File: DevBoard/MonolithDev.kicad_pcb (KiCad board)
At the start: 2 copper layers, 0 parts

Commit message: Dev board: board setup (175x115, 4L 0.8 mm), netlist loaded, PDFN fix
- Board: 175 x 115 mm (the four holders need ~96 x 110), 4 layers 0.8 mm,
  2 oz outer / 1 oz inner, ENIG stack-up; six M3 board-only holes; outline
  broken for the two USB-C notches, J401/J501 placed and locked on the right edge
- JLC rules, via/track presets, net classes (HighCurrent, Power, GND,
  GateDrive) and custom rules in MonolithDev.kicad_dru (tools/setup_board.py)
- Netlist loaded with tools/netlist_to_board.py (the MCP sync merged the two
  ports' nets); kicad-cli parity check reports 0 issues
- Q101/Q102: AGM404AP1 is a 3.3x3.3 PDFN, not TDSON-8 (5x6); new footprint
- USB-C signal pads moved 0.2 mm in from the notch for JLC's edge clearance
- Production notes: notch is 5.65 mm deep (not 4.7), flange sticks out ~1.95 mm

Co-Authored-By: Claude Opus 5.5 <noreply@anthropic.com>
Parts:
- added BT101, BT102, BT103, BT104: BH-21700-B1BJ001, MonolithDev:BatteryHolder_MYOUNG_BH-21700-B1BJ001, F.Cu at (0.00, 0.00)
- added C101, C102, C103, C104, C412, C413, C440, C512, C513, C540: 0.1u 25V, Capacitor_SMD:C_0603_1608Metric, F.Cu at (0.00, 0.00)
- added C105: 2.2u 25V, Capacitor_SMD:C_0603_1608Metric, F.Cu at (0.00, 0.00)
- added C106, C202, C203, C308, C309, C310, C311: 0.1u, Capacitor_SMD:C_0603_1608Metric, F.Cu at (0.00, 0.00)
- added C107, C108, C415, C416, C418, C419, C430, C438, C446, C515, C516, C518, C519, C530, C538, C546: 0.1u 50V, Capacitor_SMD:C_0603_1608Metric, F.Cu at (0.00, 0.00)
- added C201: 22n DNP, Capacitor_SMD:C_0603_1608Metric, F.Cu at (0.00, 0.00)
- added C204: 1u 50V, Capacitor_SMD:C_0805_2012Metric, F.Cu at (0.00, 0.00)
- added C205: 2.2u 10V, Capacitor_SMD:C_0603_1608Metric, F.Cu at (0.00, 0.00)
- added C206: 2.2u 50V, Capacitor_SMD:C_0805_2012Metric, F.Cu at (0.00, 0.00)
- added C207: 22u 10V, Capacitor_SMD:C_0805_2012Metric, F.Cu at (0.00, 0.00)
- added C301: 4.7u, Capacitor_SMD:C_0603_1608Metric, F.Cu at (0.00, 0.00)
- added C302, C303, C304, C408, C508: 0.1u, Capacitor_SMD:C_0402_1005Metric, F.Cu at (0.00, 0.00)
- added C401, C402, C501, C502: 330p, Capacitor_SMD:C_0402_1005Metric, F.Cu at (0.00, 0.00)
- added C403, C404, C503, C504: 10u 25V, Capacitor_SMD:C_0805_2012Metric, F.Cu at (0.00, 0.00)
- added C405, C505: 10u 10V, Capacitor_SMD:C_0603_1608Metric, F.Cu at (0.00, 0.00)
- added C406, C506: 4.7u 50V, Capacitor_SMD:C_0805_2012Metric, F.Cu at (0.00, 0.00)
- added C407, C507: 10u 10V, Capacitor_SMD:C_0805_2012Metric, F.Cu at (0.00, 0.00)
- added C409, C509: 1u 35V (VAC), Capacitor_SMD:C_0603_1608Metric, F.Cu at (0.00, 0.00)
- added C410, C411, C510, C511: 4.7u 16V, Capacitor_SMD:C_0805_2012Metric, F.Cu at (0.00, 0.00)
- added C414, C417, C514, C517: 0.47u 25V, Capacitor_SMD:C_0603_1608Metric, F.Cu at (0.00, 0.00)
- added C420, C421, C422, C423, C424, C425, C426, C427, C428, C429, C520, C521, C522, C523, C524, C525, C526, C527, C528, C529: 22u 35V, Capacitor_SMD:C_1210_3225Metric, F.Cu at (0.00, 0.00)
- added C431, C432, C433, C434, C435, C436, C437, C531, C532, C533, C534, C535, C536, C537: 47u 25V, Capacitor_SMD:C_1210_3225Metric, F.Cu at (0.00, 0.00)
- added C439, C539: 33n, Capacitor_SMD:C_0603_1608Metric, F.Cu at (0.00, 0.00)
- added C441, C442, C541, C542: 22u 35V, Capacitor_SMD:C_1206_3216Metric, F.Cu at (0.00, 0.00)
- added C443, C543: 220u 16V, Capacitor_SMD:CP_Elec_6.3x7.7, F.Cu at (0.00, 0.00)
- added C444, C445, C544, C545: 10u 50V, Capacitor_SMD:C_1206_3216Metric, F.Cu at (0.00, 0.00)
- added D101: BAT54WS, Diode_SMD:D_SOD-323, F.Cu at (0.00, 0.00)
- added D301: Green status, LED_SMD:LED_0603_1608Metric, F.Cu at (0.00, 0.00)
- added D401, D501: SMAJ22A, Diode_SMD:D_SMA, F.Cu at (0.00, 0.00)
- added D402, D403, D502, D503: ESD2CAN24DBZRQ1, Package_TO_SOT_SMD:SOT-23, F.Cu at (0.00, 0.00)
- added F101: 8A 32V, Fuse:Fuse_1206_3216Metric, F.Cu at (0.00, 0.00)
- added H1: MountingHole_3.2mm_M3, MountingHole:MountingHole_3.2mm_M3, F.Cu at (54.0, 54.0)
- added H2: MountingHole_3.2mm_M3, MountingHole:MountingHole_3.2mm_M3, F.Cu at (151.0, 54.0)
- added H3: MountingHole_3.2mm_M3, MountingHole:MountingHole_3.2mm_M3, F.Cu at (221.0, 54.0)
- added H4: MountingHole_3.2mm_M3, MountingHole:MountingHole_3.2mm_M3, F.Cu at (54.0, 161.0)
- added H5: MountingHole_3.2mm_M3, MountingHole:MountingHole_3.2mm_M3, F.Cu at (151.0, 161.0)
- added H6: MountingHole_3.2mm_M3, MountingHole:MountingHole_3.2mm_M3, F.Cu at (221.0, 161.0)
- added J101: Pack (welded 4S) - use instead of holders, TerminalBlock_Phoenix:TerminalBlock_Phoenix_MKDS-1,5-5-5.08_1x05_P5.08mm_Horizontal, F.Cu at (0.00, 0.00)
- added J102: Cell NTC 10k 103AT, Connector_PinHeader_2.54mm:PinHeader_1x02_P2.54mm_Vertical, F.Cu at (0.00, 0.00)
- added J103: EV2400 SMBus, Connector_PinHeader_2.54mm:PinHeader_1x03_P2.54mm_Vertical, F.Cu at (0.00, 0.00)
- added J201: SMA OUT_LO, Connector_Coaxial:SMA_Amphenol_132289_EdgeMount, F.Cu at (0.00, 0.00)
- added J202: SMA OUT_HI, Connector_Coaxial:SMA_Amphenol_132289_EdgeMount, F.Cu at (0.00, 0.00)
- added J301: SWD, Connector_PinHeader_1.27mm:PinHeader_2x05_P1.27mm_Vertical, F.Cu at (0.00, 0.00)
- added J302: UART debug, Connector_PinHeader_2.54mm:PinHeader_1x03_P2.54mm_Vertical, F.Cu at (0.00, 0.00)
- added J303: Spare GPIO, Connector_PinHeader_2.54mm:PinHeader_1x07_P2.54mm_Vertical, F.Cu at (0.00, 0.00)
- added J401: TYPE-C 16PCB0.8 IP68, MonolithDev:USB_C_Receptacle_ShouHan_TYPE-C_16PCB0.8_IP68, F.Cu at (225.0, 85.0)
- added J402, J502: I2CC logic analyzer, Connector_PinHeader_2.54mm:PinHeader_1x03_P2.54mm_Vertical, F.Cu at (0.00, 0.00)
- added J501: TYPE-C 16PCB0.8 IP68, MonolithDev:USB_C_Receptacle_ShouHan_TYPE-C_16PCB0.8_IP68, F.Cu at (225.0, 128.0)
- added JP201: AMP_EN, Connector_PinHeader_2.54mm:PinHeader_1x02_P2.54mm_Vertical, F.Cu at (0.00, 0.00)
- added JP202: Meas. section power, Connector_PinHeader_2.54mm:PinHeader_1x02_P2.54mm_Vertical, F.Cu at (0.00, 0.00)
- added L201: 10u, Inductor_SMD:L_Bourns-SRN4018, F.Cu at (0.00, 0.00)
- added L401, L501: 2.2u, Inductor_SMD:L_Coilcraft_XAL7030-222, F.Cu at (0.00, 0.00)
- added L402, L502: 3.3u, Inductor_SMD:L_Bourns_SRP5030T, F.Cu at (0.00, 0.00)
- added Q101, Q102: AGM404AP1, MonolithDev:AGM_PDFN-8_3.3x3.3mm_P0.65mm, F.Cu at (0.00, 0.00)
- added Q401, Q402, Q501, Q502: IAUC45N04S6L063H, MonolithDev:Infineon_PG-TDSON-8-57_HalfBridge, F.Cu at (0.00, 0.00)
- added R1, R2, R202, R203, R204, R205, R3, R307, R4: 0R, Resistor_SMD:R_0603_1608Metric, F.Cu at (0.00, 0.00)
- added R101, R102, R103, R104, R105, R106, R107, R108, R115, R116: 100, Resistor_SMD:R_0603_1608Metric, F.Cu at (0.00, 0.00)
- added R109, R111: 5.1k, Resistor_SMD:R_0603_1608Metric, F.Cu at (0.00, 0.00)
- added R110, R112: 10M, Resistor_SMD:R_0603_1608Metric, F.Cu at (0.00, 0.00)
- added R113, R302, R404, R417, R421, R422, R423, R504, R517, R521, R522, R523: 10k, Resistor_SMD:R_0603_1608Metric, F.Cu at (0.00, 0.00)
- added R114, R206, R208, R432, R532: 100k, Resistor_SMD:R_0603_1608Metric, F.Cu at (0.00, 0.00)
- added R201: 10R 1% 0.5W, Resistor_SMD:R_1206_3216Metric, F.Cu at (0.00, 0.00)
- added R207, R301, R401, R501: 0R, Resistor_SMD:R_0805_2012Metric, F.Cu at (0.00, 0.00)
- added R303: 0R, Resistor_SMD:R_0402_1005Metric, F.Cu at (0.00, 0.00)
- added R304, R305: 4.7k, Resistor_SMD:R_0603_1608Metric, F.Cu at (0.00, 0.00)
- added R306: 1k, Resistor_SMD:R_0603_1608Metric, F.Cu at (0.00, 0.00)
- added R308, R309, R310, R311, R411, R419, R511, R519: 10.0k 0.1%, Resistor_SMD:R_0805_2012Metric, F.Cu at (0.00, 0.00)
- added R402, R403, R502, R503: 3.3k, Resistor_SMD:R_0603_1608Metric, F.Cu at (0.00, 0.00)
- added R405, R406, R407, R408, R505, R506, R507, R508: DNP, Resistor_SMD:R_0603_1608Metric, F.Cu at (0.00, 0.00)
- added R409, R509: 137k 0.1%, Resistor_SMD:R_0805_2012Metric, F.Cu at (0.00, 0.00)
- added R410, R412, R510, R512: 40.2k 0.1%, Resistor_SMD:R_0805_2012Metric, F.Cu at (0.00, 0.00)
- added R413, R416, R513, R516: 5.11k 0.1%, Resistor_SMD:R_0603_1608Metric, F.Cu at (0.00, 0.00)
- added R414, R514: 3.65k 0.1%, Resistor_SMD:R_0603_1608Metric, F.Cu at (0.00, 0.00)
- added R415, R515: 1.74k 0.1%, Resistor_SMD:R_0603_1608Metric, F.Cu at (0.00, 0.00)
- added R418, R518: 100k 0.1%, Resistor_SMD:R_0805_2012Metric, F.Cu at (0.00, 0.00)
- added R420, R425, R426, R428, R429, R520, R525, R526, R528, R529: 10R, Resistor_SMD:R_0603_1608Metric, F.Cu at (0.00, 0.00)
- added R424, R524: 5m 2W (RAC), Resistor_SMD:R_2010_5025Metric, F.Cu at (0.00, 0.00)
- added R427, R527: 5m 2W (RBAT), Resistor_SMD:R_2010_5025Metric, F.Cu at (0.00, 0.00)
- added R430, R530: Link 10A, MonolithDev:NetTie-2_SMD_3x3mm_Bridge3mm, F.Cu at (0.00, 0.00)
- added R431, R531: 0R, Resistor_SMD:R_1206_3216Metric, F.Cu at (0.00, 0.00)
- added R433, R533: 105k 0.1%, Resistor_SMD:R_0805_2012Metric, F.Cu at (0.00, 0.00)
- added R434, R534: 20.0k 0.1%, Resistor_SMD:R_0805_2012Metric, F.Cu at (0.00, 0.00)
- added RS101: 1m 1% 2W, Resistor_SMD:R_2512_6332Metric, F.Cu at (0.00, 0.00)
- added TH301, TH302, TH303, TH304, TH401, TH501: 10k B3435, Resistor_SMD:R_0603_1608Metric, F.Cu at (0.00, 0.00)
- added TP101: CELL_P, TestPoint:TestPoint_Keystone_5000-5004_Miniature, F.Cu at (0.00, 0.00)
- added TP102: CELL_N, TestPoint:TestPoint_Keystone_5000-5004_Miniature, F.Cu at (0.00, 0.00)
- added TP103: CELL1, TestPoint:TestPoint_Keystone_5000-5004_Miniature, F.Cu at (0.00, 0.00)
- added TP104: CELL2, TestPoint:TestPoint_Keystone_5000-5004_Miniature, F.Cu at (0.00, 0.00)
- added TP105: CELL3, TestPoint:TestPoint_Keystone_5000-5004_Miniature, F.Cu at (0.00, 0.00)
- added TP106: PACK_P, TestPoint:TestPoint_Keystone_5000-5004_Miniature, F.Cu at (0.00, 0.00)
- added TP107: GAUGE_BTP, TestPoint:TestPoint_Keystone_5000-5004_Miniature, F.Cu at (0.00, 0.00)
- added TP201: OUT_LO, TestPoint:TestPoint_Keystone_5000-5004_Miniature, F.Cu at (0.00, 0.00)
- added TP202: OUT_HI, TestPoint:TestPoint_Keystone_5000-5004_Miniature, F.Cu at (0.00, 0.00)
- added TP203: GND, TestPoint:TestPoint_Keystone_5000-5004_Miniature, F.Cu at (0.00, 0.00)
- added TP204: PACK_LP, TestPoint:TestPoint_Keystone_5000-5004_Miniature, F.Cu at (0.00, 0.00)
- added TP205: PG_3V3, TestPoint:TestPoint_Keystone_5000-5004_Miniature, F.Cu at (0.00, 0.00)
- added TP301: 3V3, TestPoint:TestPoint_Keystone_5000-5004_Miniature, F.Cu at (0.00, 0.00)
- added TP302: SDA, TestPoint:TestPoint_Keystone_5000-5004_Miniature, F.Cu at (0.00, 0.00)
- added TP303: SCL, TestPoint:TestPoint_Keystone_5000-5004_Miniature, F.Cu at (0.00, 0.00)
- added TP304: IRQ1, TestPoint:TestPoint_Keystone_5000-5004_Miniature, F.Cu at (0.00, 0.00)
- added TP305: IRQ2, TestPoint:TestPoint_Keystone_5000-5004_Miniature, F.Cu at (0.00, 0.00)
- added TP401, TP501: VBUS, TestPoint:TestPoint_Keystone_5000-5004_Miniature, F.Cu at (0.00, 0.00)
- added TP402, TP502: PPHV, TestPoint:TestPoint_Keystone_5000-5004_Miniature, F.Cu at (0.00, 0.00)
- added TP403, TP503: PP5V, TestPoint:TestPoint_Keystone_5000-5004_Miniature, F.Cu at (0.00, 0.00)
- added TP404, TP504: REGN, TestPoint:TestPoint_Keystone_5000-5004_Miniature, F.Cu at (0.00, 0.00)
- added TP405, TP505: SW1, TestPoint:TestPoint_Keystone_5000-5004_Miniature, F.Cu at (0.00, 0.00)
- added TP406, TP506: SW2, TestPoint:TestPoint_Keystone_5000-5004_Miniature, F.Cu at (0.00, 0.00)
- added TP407, TP507: I2CC_SDA, TestPoint:TestPoint_Keystone_5000-5004_Miniature, F.Cu at (0.00, 0.00)
- added TP408, TP508: I2CC_SCL, TestPoint:TestPoint_Keystone_5000-5004_Miniature, F.Cu at (0.00, 0.00)
- added TP409, TP509: STAT1, TestPoint:TestPoint_Keystone_5000-5004_Miniature, F.Cu at (0.00, 0.00)
- added TP410, TP510: STAT2, TestPoint:TestPoint_Keystone_5000-5004_Miniature, F.Cu at (0.00, 0.00)
- added TP411, TP511: PG, TestPoint:TestPoint_Keystone_5000-5004_Miniature, F.Cu at (0.00, 0.00)
- added U101: BQ40Z50RSMR-R2, Package_DFN_QFN:VQFN-32-1EP_4x4mm_P0.4mm_EP2.8x2.8mm, F.Cu at (0.00, 0.00)
- added U201: INA190A5IDDFR, Package_TO_SOT_SMD:TSOT-23-8, F.Cu at (0.00, 0.00)
- added U202: INA190A1IDDFR, Package_TO_SOT_SMD:TSOT-23-8, F.Cu at (0.00, 0.00)
- added U203: TPS70950DBVR, Package_TO_SOT_SMD:SOT-23-5, F.Cu at (0.00, 0.00)
- added U204: TPS62177DQCR, Package_SON:WSON-10-1EP_2x3mm_P0.5mm_EP0.84x2.4mm, F.Cu at (0.00, 0.00)
- added U301: STM32WB1MMC, MonolithDev:ST_LGA-77_STM32WB1MMC_6.5x10mm, F.Cu at (0.00, 0.00)
- added U401, U501: TPS25751DREFR, Package_DFN_QFN:Texas_REF0038A_WQFN-38-2EP_6x4mm_P0.4, F.Cu at (0.00, 0.00)
- added U402, U502: M24512-DFMC6TG, MonolithDev:ST_UFDFPN-8-1EP_2x3mm_P0.5mm_EP1.2x1.4mm, F.Cu at (0.00, 0.00)
- added U403, U503: BQ25756RRVR, MonolithDev:TI_VQFN-36-1EP_RRV0036A_5x6mm_P0.5mm, F.Cu at (0.00, 0.00)
- added U404, U504: TPS62933DRLR, Package_TO_SOT_SMD:SOT-583-8, F.Cu at (0.00, 0.00)
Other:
- board outline added: 175 x 115 mm
- copper layers 2 -> 4

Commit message: Dev board: first-pass placement (196x115), DRC clean before routing
- tools/place_parts.py: mechanical (outline, holes, USB-C), hand placement of
  holders, gauge core and VC filter ladder, sleep-current section, MCU and
  both charger power trains; auto placement of the small parts next to the
  pins they serve; silkscreen labels (P1/P2 test points, USB 1/2)
- Board widened to 196 mm: holder courtyards collided with the corner holes
- TPS25751 footprint copy with the PPHV/VBUS pad gap opened to 0.15 mm (2 oz)
- Rules: HighCurrent/Power pad clearance 0.15 mm; 0.25 mm only between
  high-current copper and small-signal copper
- DRC: 0 placement/clearance/silk issues, 0 parity issues; unrouted only

Co-Authored-By: Claude Opus 5.5 <noreply@anthropic.com>
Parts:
- U401, U501: footprint Package_DFN_QFN:Texas_REF0038A_WQFN-38-2EP_6x4mm_P0.4 -> MonolithDev:TI_WQFN-38-2EP_REF0038A_6x4mm_P0.4mm_2oz
- moved TP202 281.2 mm to (233.5, 156.7)
- moved J202 279.8 mm to (228.0, 162.2), turned to -90 degrees
- moved TP503 279.1 mm to (241.5, 139.9)
- moved L201 277.5 mm to (236.0, 146.0)
- moved R514 276.5 mm to (243.2, 131.5), turned to 90 degrees
- moved C207 274.8 mm to (235.3, 142.0)
- moved R205 274.0 mm to (224.2, 157.4)
- moved C516 273.9 mm to (241.8, 128.6)
- moved R533 272.8 mm to (241.9, 126.1)
- moved L502 272.6 mm to (238.0, 133.0)
- moved U204 272.4 mm to (230.0, 146.0)
- moved TP203 271.5 mm to (225.0, 152.0)
- moved R208 269.7 mm to (226.8, 146.0), turned to 90 degrees
- moved TP205 269.5 mm to (229.0, 142.0)
- moved C539 269.1 mm to (231.7, 136.8)
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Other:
- board size 175 x 115 mm -> 196 x 115 mm
- board text added: "P1 I2CC_SCL"
- board text added: "P1 I2CC_SDA"
- board text added: "P1 PG"
- board text added: "P1 PP5V"
- board text added: "P1 PPHV"
- board text added: "P1 REGN"
- board text added: "P1 STAT1"
- board text added: "P1 STAT2"
- board text added: "P1 SW1"
- board text added: "P1 SW2"
- board text added: "P1 VBUS"
- board text added: "P2 I2CC_SCL"
- board text added: "P2 I2CC_SDA"
- board text added: "P2 PG"
- board text added: "P2 PP5V"
- board text added: "P2 PPHV"
- board text added: "P2 REGN"
- board text added: "P2 STAT1"
- board text added: "P2 STAT2"
- board text added: "P2 SW1"
- board text added: "P2 SW2"
- board text added: "P2 VBUS"
- board text added: "USB 1"
- board text added: "USB 2"

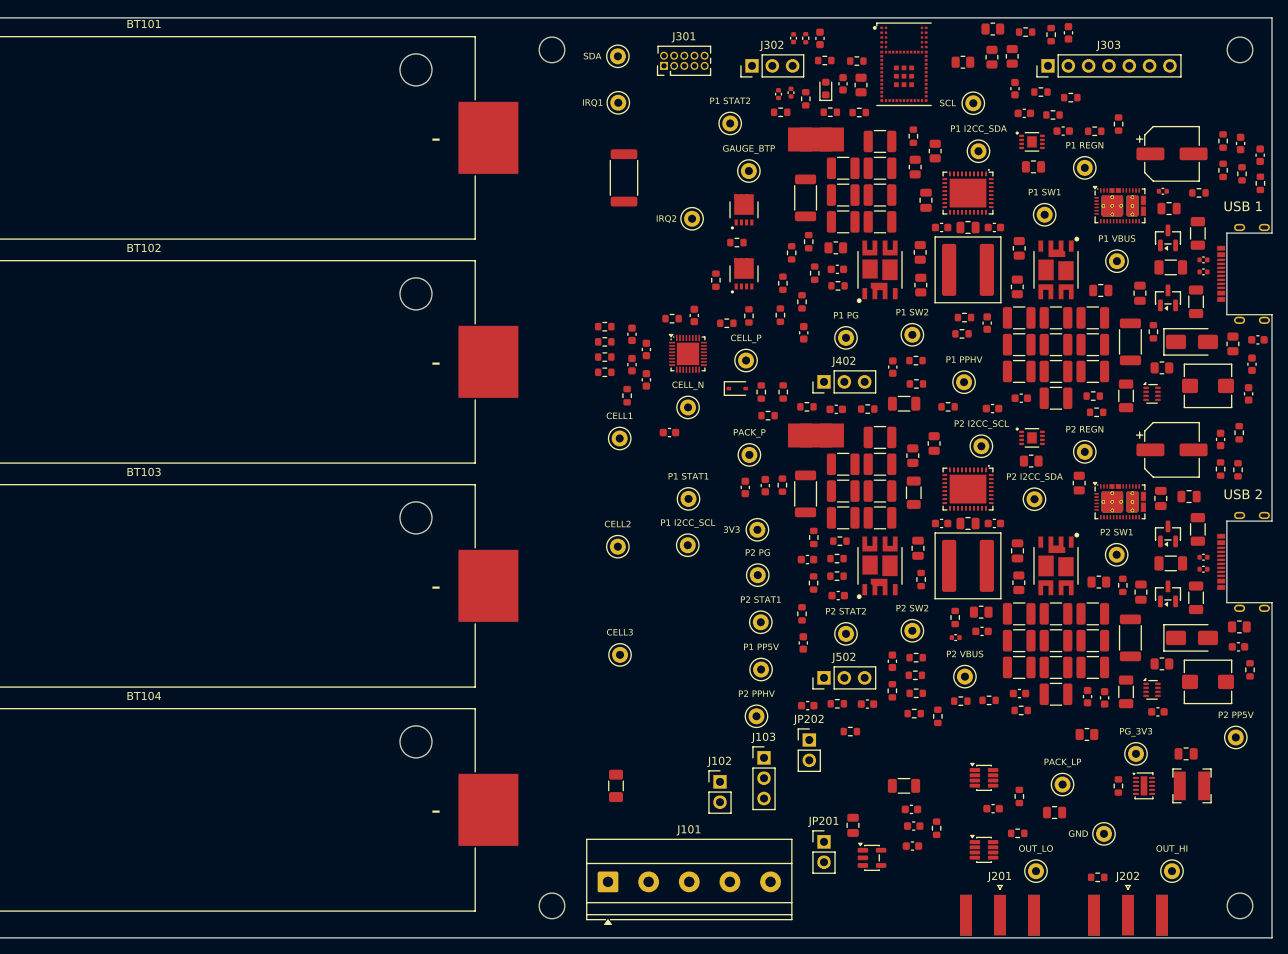
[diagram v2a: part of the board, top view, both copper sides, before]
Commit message: Dev board rev A4: design-review fixes, polymer bulk, charge inhibit
Schematic design review (three reviewers, cross-challenged) in
docs/devboard/schematic-review-2026-10-12.md, and its fixes:
- U203 TPS70950 EN no longer tied to PACK_P (would destroy it)
- ICHG 17.8k: 2.8 A per port (was 9.8 A, above the cells' 5.6 A)
- U101 footprint from TI RSM0032A (1.4 mm thermal pad, was 2.8 mm)
- D+/D- ESD now 5 V PESD5V0S2BT (TPS25751 GPIO4/5 are rated 6 V)
- R101-R104 1206, F101 and J101 DNP, DNP gate parts on Q102
- BTP_INT buffered by a 2N7002; SMBus pull-ups on a removable 0R
- Wake button, bench PACK_P header, reset, BOOT0/3V3_SLEEP pads,
  J303 series resistors, IRQ pull-ups, vertical SMAs, BOM ratings

Open-question decisions: CHG_INH (PB8 -> each BQ25756 CE) lets the
MCU stop charging independently of the TPS25751; J103 in EV2400
SMBus pin order; "fit cells before USB" silkscreen.

Charger bulk banks now one solid polymer cap plus the MLCCs at the
FETs (16 fewer MLCCs). PWR_FLAGs moved to where each rail is sourced.
Board: footprints swapped/added and placed, DRC clean before routing.

Co-Authored-By: Claude Opus 5.5 <noreply@anthropic.com>
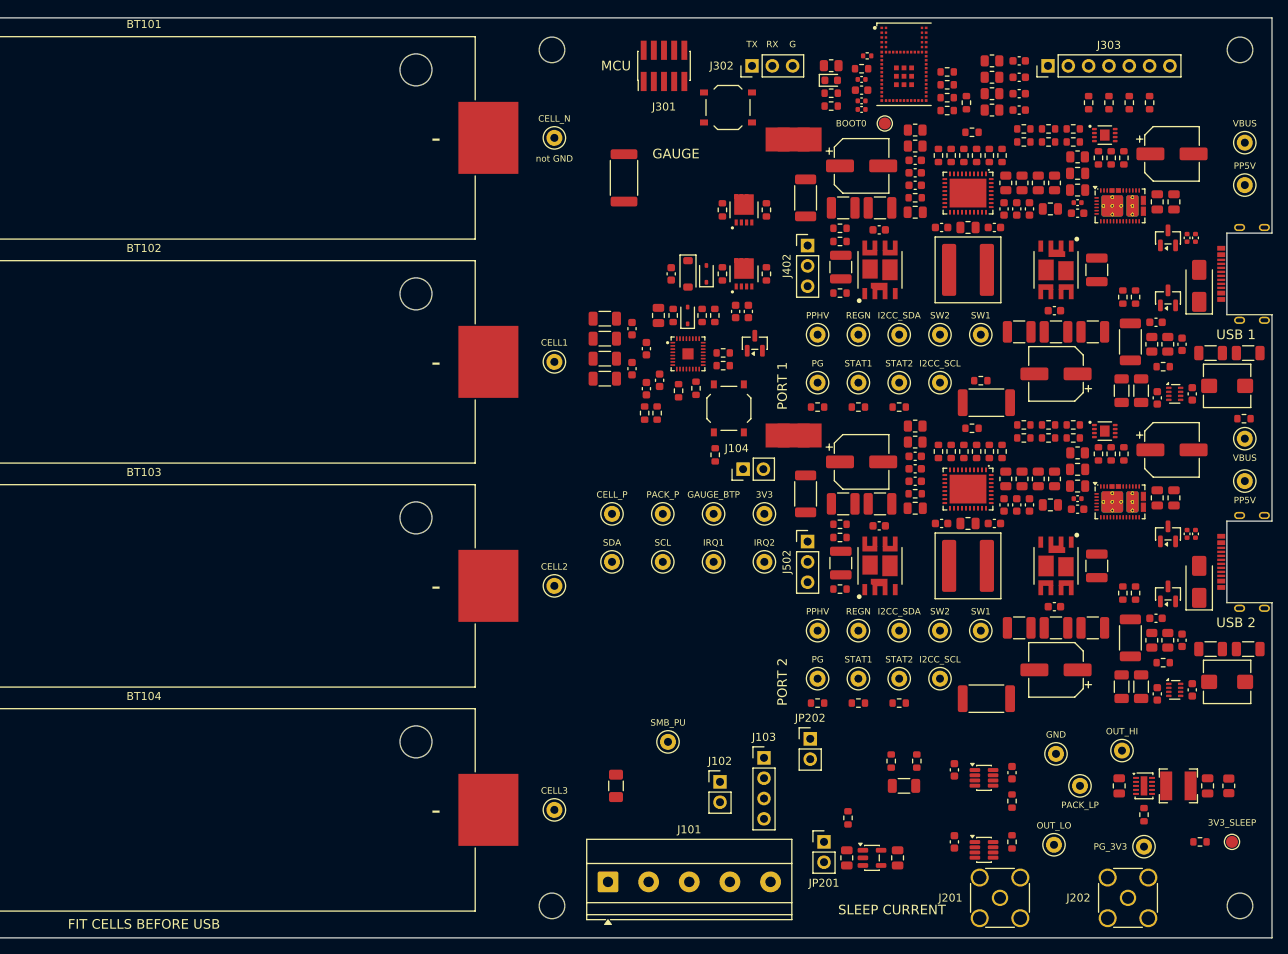
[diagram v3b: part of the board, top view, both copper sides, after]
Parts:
- removed C422, C425, C426, C428, C429, C522, C525, C526, C528, C529: 22u 35V, Capacitor_SMD:C_1210_3225Metric
- removed C433, C436, C437, C533, C536, C537: 47u 25V, Capacitor_SMD:C_1210_3225Metric
- added C109: 0.1u 50V, Capacitor_SMD:C_0603_1608Metric, F.Cu at (170.9, 82.0)
- added C447: 10p, Capacitor_SMD:C_0603_1608Metric, F.Cu at (231.5, 88.0)
- added C547: 10p, Capacitor_SMD:C_0603_1608Metric, F.Cu at (231.5, 125.0)
- added D102: 1N4148WS, Diode_SMD:D_SOD-323, F.Cu at (175.3, 82.0)
- added D103: BZT52C15, Diode_SMD:D_SOD-123, F.Cu at (173.0, 82.0)
- added J104: Bench PACK_P, Connector_PinHeader_2.54mm:PinHeader_1x02_P2.54mm_Vertical, F.Cu at (179.9, 106.4)
- added Q103: 2N7002, Package_TO_SOT_SMD:SOT-23, F.Cu at (181.3, 90.7)
- added R117: 470k, Resistor_SMD:R_0603_1608Metric, F.Cu at (171.8, 96.6)
- added R118: 4.7k, Resistor_SMD:R_0603_1608Metric, F.Cu at (176.4, 104.6)
- added R312: 0R, Resistor_SMD:R_0603_1608Metric, F.Cu at (207.8, 60.6)
- added R313: 100k, Resistor_SMD:R_0603_1608Metric, F.Cu at (237.0, 153.0)
- added R314: 100k, Resistor_SMD:R_0603_1608Metric, F.Cu at (205.4, 56.8)
- added R315: 100k, Resistor_SMD:R_0603_1608Metric, F.Cu at (205.4, 58.4)
- added R316: 1k, Resistor_SMD:R_0603_1608Metric, F.Cu at (223.1, 60.6)
- added R317: 1k, Resistor_SMD:R_0603_1608Metric, F.Cu at (225.6, 60.6)
- added R318: 1k, Resistor_SMD:R_0603_1608Metric, F.Cu at (228.2, 60.6)
- added R319: 1k, Resistor_SMD:R_0603_1608Metric, F.Cu at (230.7, 60.6)
- added R435: 1k, Resistor_SMD:R_0603_1608Metric, F.Cu at (208.5, 64.3)
- added R535: 1k, Resistor_SMD:R_0603_1608Metric, F.Cu at (208.5, 101.3)
- added SW101: WAKE, Button_Switch_SMD:SW_Push_1P1T_XKB_TS-1187A, F.Cu at (178.1, 98.8)
- added SW301: RESET, Button_Switch_SMD:SW_Push_1P1T_XKB_TS-1187A, F.Cu at (178.0, 61.2)
- added TP306: BOOT0, TestPoint:TestPoint_Pad_D1.5mm, F.Cu at (197.6, 63.2)
- added TP307: 3V3_SLEEP, TestPoint:TestPoint_Pad_D1.5mm, F.Cu at (241.0, 153.0)
- added TP308: SMB_PU, TestPoint:TestPoint_Keystone_5000-5004_Miniature, F.Cu at (170.5, 140.5)
- C105: value 2.2u 25V -> 2.2u 50V; footprint Capacitor_SMD:C_0603_1608Metric -> Capacitor_SMD:C_0805_2012Metric
- C106, C202, C203, C302, C303, C304, C308, C309, C310, C311, C408, C508: value 0.1u -> 0.1u 50V
- C205: value 2.2u 10V -> 4.7u 25V; footprint Capacitor_SMD:C_0603_1608Metric -> Capacitor_SMD:C_0805_2012Metric
- C301: value 4.7u -> 4.7u 16V
- C401, C402, C501, C502: value 330p -> 330p 50V
- C409, C509: value 1u 35V (VAC) -> 1u 50V (VAC); footprint Capacitor_SMD:C_0603_1608Metric -> Capacitor_SMD:C_0805_2012Metric
- C421, C521: value 22u 35V -> 68u 35V; footprint Capacitor_SMD:C_1210_3225Metric -> Capacitor_SMD:CP_Elec_6.3x5.8
- C432, C532: value 47u 25V -> 100u 25V; footprint Capacitor_SMD:C_1210_3225Metric -> Capacitor_SMD:CP_Elec_6.3x5.8
- D403, D503: value ESD2CAN24DBZRQ1 -> PESD5V0S2BT
- J103: footprint Connector_PinHeader_2.54mm:PinHeader_1x03_P2.54mm_Vertical -> Connector_PinHeader_2.54mm:PinHeader_1x04_P2.54mm_Vertical
- J201, J202: footprint Connector_Coaxial:SMA_Amphenol_132289_EdgeMount -> Connector_Coaxial:SMA_Amphenol_132134_Vertical
- J301: footprint Connector_PinHeader_1.27mm:PinHeader_2x05_P1.27mm_Vertical -> Connector_PinHeader_1.27mm:PinHeader_2x05_P1.27mm_Vertical_SMD
- R101, R102, R103, R104: footprint Resistor_SMD:R_0603_1608Metric -> Resistor_SMD:R_1206_3216Metric
- R201: value 10R 1% 0.5W -> 10R 1%
- R204, R205: value 0R -> 49.9
- R413, R513: value 5.11k 0.1% -> 17.8k 0.1%
- R431, R531: footprint Resistor_SMD:R_1206_3216Metric -> Resistor_SMD:R_2512_6332Metric
- R433, R533: value 105k 0.1% -> 107k 0.1%
- U101: footprint Package_DFN_QFN:VQFN-32-1EP_4x4mm_P0.4mm_EP2.8x2.8mm -> MonolithDev:TI_RSM0032A_VQFN-32_4x4mm_P0.4mm_EP1.4x1.4mm
- moved TP403 85.6 mm to (242.6, 70.9)
- moved TP303 69.2 mm to (169.8, 118.0)
- moved TH302 67.0 mm to (192.0, 121.4), turned to 180 degrees
- moved TH303 65.9 mm to (242.5, 100.1)
- moved TP302 63.2 mm to (163.5, 118.0)
- moved TP304 58.6 mm to (176.2, 118.0)
- moved R514 47.6 mm to (204.3, 104.2)
- moved TP501 45.9 mm to (242.6, 102.6)
- moved TH304 44.1 mm to (209.6, 95.3), turned to 180 degrees
- moved TP305 43.8 mm to (182.6, 118.0)
- moved TP107 43.1 mm to (176.2, 112.0)
- moved R504 41.7 mm to (227.5, 104.5), turned to -90 degrees
- moved R3 40.2 mm to (221.2, 100.9), turned to 180 degrees
- moved TH301 40.0 mm to (192.0, 84.4), turned to 180 degrees
- moved TP410 38.7 mm to (199.4, 95.6)
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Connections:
- J103 pad 1: SCL -> GND
- J103 pad 2: SDA -> SCL
- J103 pad 3: GND -> SDA
- J303 pad 3: /MCU and NTCs/NTC_EN -> /MCU and NTCs/J303_NTC_EN
- J303 pad 4: EN_5V1 -> /MCU and NTCs/J303_EN_5V1
- J303 pad 5: EN_5V2 -> /MCU and NTCs/J303_EN_5V2
- J303 pad 6: /MCU and NTCs/PB8 -> /MCU and NTCs/J303_CHG_INH
- R304 pad 1: 3V3 -> /MCU and NTCs/SMB_PU
- R305 pad 1: 3V3 -> /MCU and NTCs/SMB_PU
- U101 pad 15: GAUGE_BTP -> /Cells and Gauge/BTP_INT
- U203 pad 3: /Sleep Current and 3V3/LDO_IN -> unconnected-(U203-EN-Pad3)
- U204 pad 4: unconnected-(U204-NC-Pad4) -> GND
- U301 pad 14: /MCU and NTCs/PB8 -> CHG_INH
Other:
- board text added: "FIT CELLS BEFORE USB"
- board text added: "G"
- board text added: "GAUGE"
- board text added: "MCU"
- board text added: "PORT 1"
- board text added: "PORT 2"
- board text added: "RX"
- board text added: "SLEEP CURRENT"
- board text added: "TX"
- board text added: "not GND"
- board text removed: "P1 I2CC_SCL"
- board text removed: "P1 I2CC_SDA"
- board text removed: "P1 PG"
- board text removed: "P1 PP5V"
- board text removed: "P1 PPHV"
- board text removed: "P1 REGN"
- board text removed: "P1 STAT1"
- board text removed: "P1 STAT2"
- board text removed: "P1 SW1"
- board text removed: "P1 SW2"
- board text removed: "P1 VBUS"
- board text removed: "P2 I2CC_SCL"
- board text removed: "P2 I2CC_SDA"
- board text removed: "P2 PG"
- board text removed: "P2 PP5V"
- board text removed: "P2 PPHV"
- board text removed: "P2 REGN"
- board text removed: "P2 STAT1"
- board text removed: "P2 STAT2"
- board text removed: "P2 SW1"
- board text removed: "P2 SW2"
- board text removed: "P2 VBUS"

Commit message: Dev board: ICHG ceiling 5.5 A per port so one port can charge at 1C
R413/R513 17.8k -> 9.09k (5.3-5.7 A hardware ceiling per port).
Both-port total stays at 5.6 A through configuration and firmware:
TPS25751 starts each charger at ICHG_REG 2.8 A, the MCU raises the
only charging port and drops it again on the other port's attach
interrupt; watchdog expiry stops charging (EN_CHG_BIT_RESET_BEHAVIOR
= 0). Documented as firmware item 14 in the review.

Co-Authored-By: Claude Opus 5.5 <noreply@anthropic.com>
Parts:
- R413, R513: value 17.8k 0.1% -> 9.09k 0.1%
